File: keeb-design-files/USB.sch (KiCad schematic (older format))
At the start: 35 parts, among them J3 USB_B, J4 S2B-PH-K-S, J5 Conn_01x02, SW71 SW_SPDT, U3 USBLC6-2SC6, U4 BQ24075, U5 NXE2S0505MC, U6 STC3100

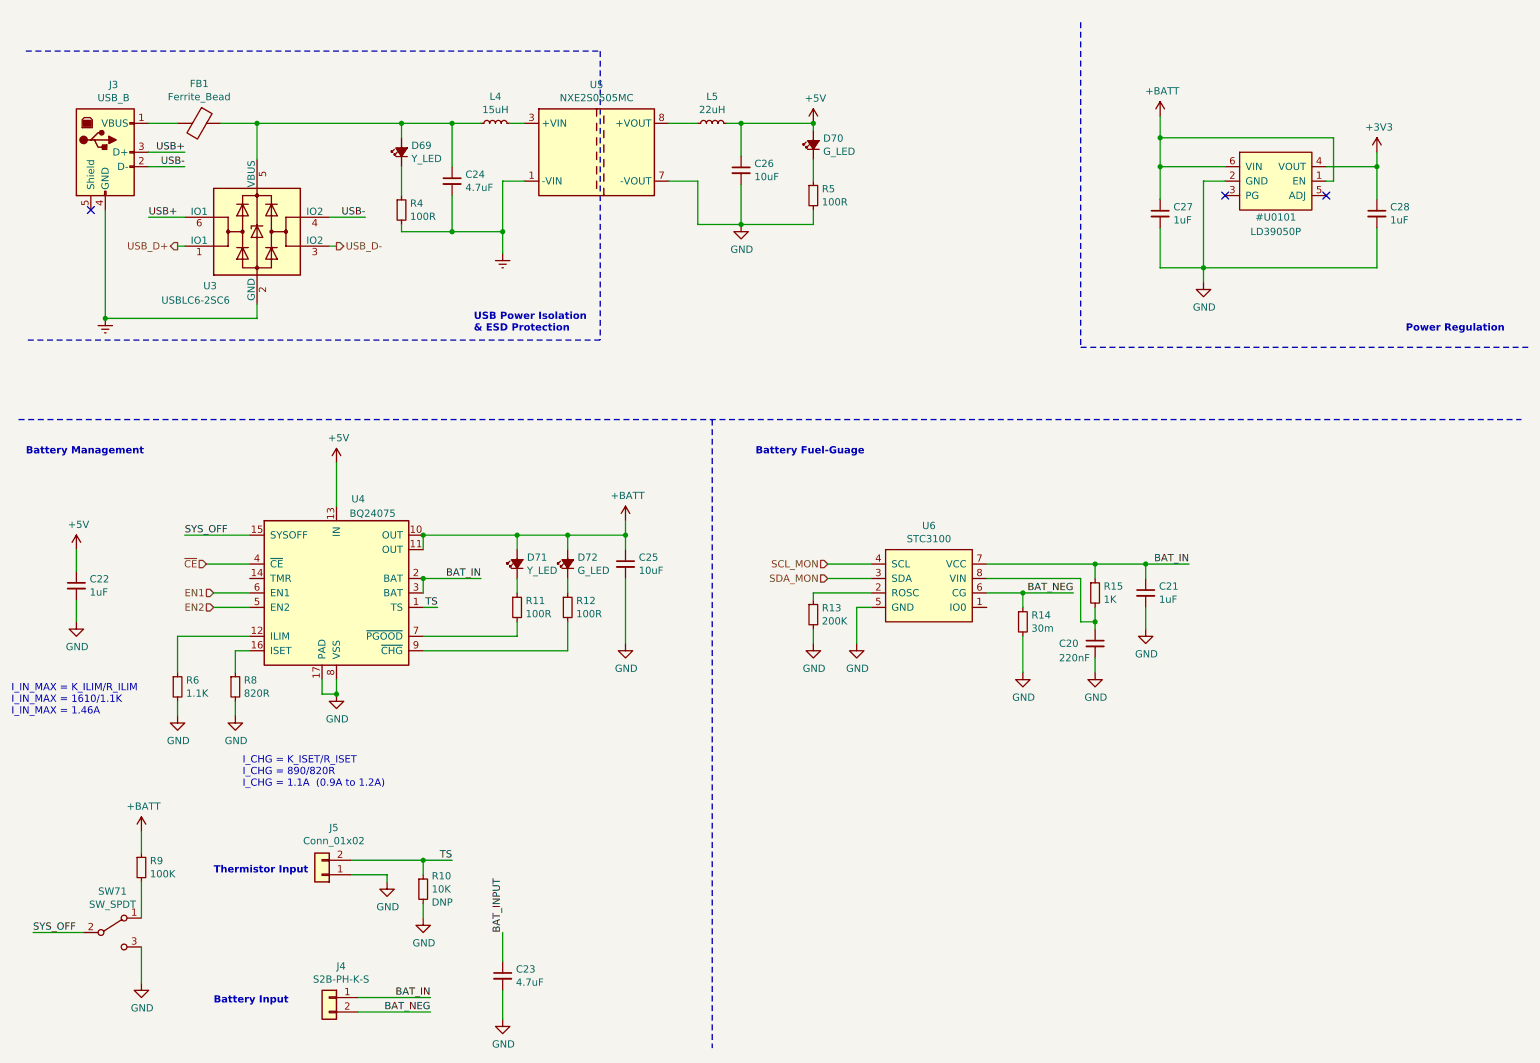
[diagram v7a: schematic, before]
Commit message: Confirm LCSC part numbers, started placement for layout
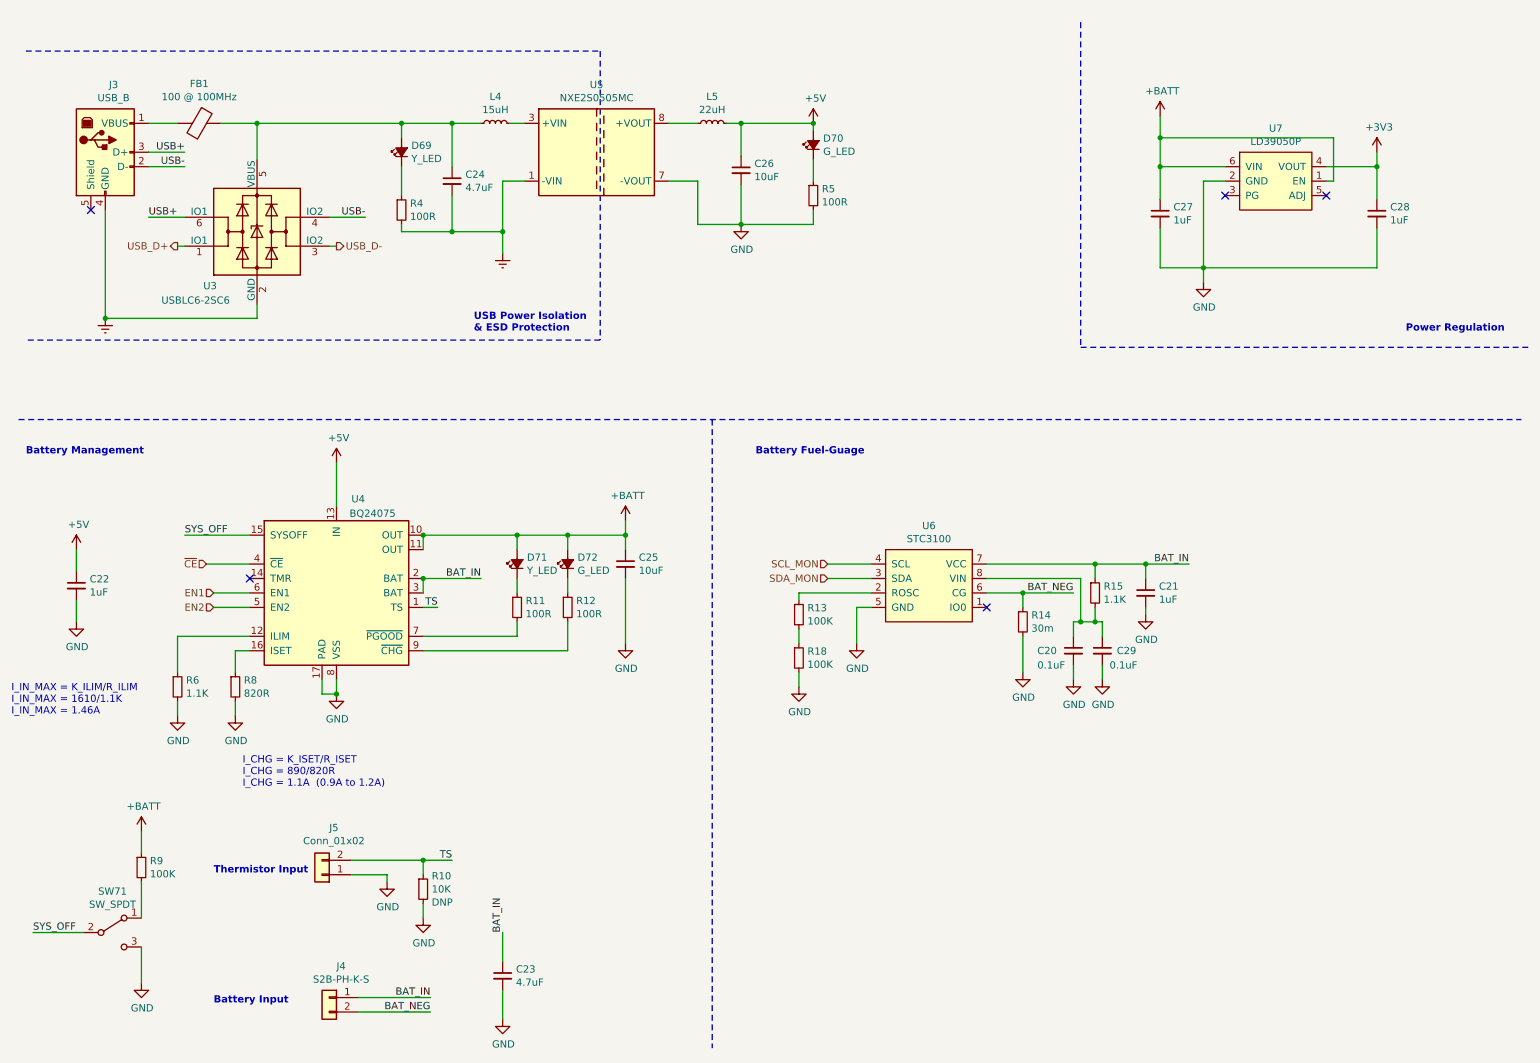
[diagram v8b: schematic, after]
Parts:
- added C29: 0.1uF, Capacitor_SMD:C_0402_1005Metric, symbol Device:C_Small
- added R18: 100K, Resistor_SMD:R_0402_1005Metric, symbol Device:R_Small
- added U7: LD39050P, Package_DFN_QFN:DFN-6-1EP_3x3mm_P0.95mm_EP1.7x2.6mm, symbol LDO:LD39050P
- C20: value 220nF -> 0.1uF; footprint (none) -> Capacitor_SMD:C_0402_1005Metric; LCSC Part Number (none) -> C1525
- C21, C22, C27, C28: footprint (none) -> Capacitor_SMD:C_0402_1005Metric; LCSC Part Number (none) -> C52923
- FB1: value Ferrite_Bead -> 100 @ 100MHz; footprint (none) -> Resistor_SMD:R_0603_1608Metric_Pad1.05x0.95mm_HandSolder
- L4, L5: footprint (none) -> Inductor_SMD:L_Bourns_SRR1260
- R10: footprint (none) -> Resistor_SMD:R_0603_1608Metric_Pad1.05x0.95mm_HandSolder
- R13: value 200K -> 100K; footprint (none) -> Resistor_SMD:R_0402_1005Metric; LCSC Part Number (none) -> C25741
- R15: value 1K -> 1.1K; footprint (none) -> Resistor_SMD:R_0402_1005Metric; LCSC Part Number (none) -> C25860
- R6, R8: footprint (none) -> Resistor_SMD:R_0402_1005Metric
- R9: footprint (none) -> Resistor_SMD:R_0402_1005Metric; LCSC Part Number (none) -> C25741
- U6: footprint (none) -> Package_DFN_QFN:DFN-8-1EP_3x3mm_P0.5mm_EP1.66x2.38mm
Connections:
- net BAT_INPUT is gone; now on net BAT_IN: C23.1
- net +3V3: now also U7.4 (VOUT)
- net +BATT: now also U7.1 (EN), U7.6 (VIN)
- net GND: now also C29.2, R18.2, U7.2 (GND); no longer R13.2
- net at C20.1, R15.2, U6.8 (VIN): now also C29.1
- new net: R13.2, R18.1
- no-connect marks 3 -> 5
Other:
- moved on the sheet: C20, R13
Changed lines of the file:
@@
 	2300 1550 2300 1300
-Wire Wire Line
-	2300 1300 3300 1300
 Wire Wire Line
 	1550 1600 1800 1600
@@
 F 0 "L4" V 4135 1300 50  0000 C CNN
 F 1 "15uH" V 4044 1300 50  0000 C CNN
-F 2 "" H 3950 1300 50  0001 C CNN
+F 2 "Inductor_SMD:L_Bourns_SRR1260" H 3950 1300 50  0001 C CNN
 F 3 "~" H 3950 1300 50  0001 C CNN
 F 4 "C132136" H 3950 1300 50  0001 C CNN "LCSC Part Number"
@@
 F 0 "L5" V 5635 1300 50  0000 C CNN
 F 1 "22uH" V 5544 1300 50  0000 C CNN
-F 2 "" H 5450 1300 50  0001 C CNN
+F 2 "Inductor_SMD:L_Bourns_SRR1260" H 5450 1300 50  0001 C CNN
 F 3 "~" H 5450 1300 50  0001 C CNN
 F 4 "C132137" H 5450 1300 50  0001 C CNN "LCSC Part Number"
@@
 	5650 2000 6150 2000
 $Comp
-L LDO:LD39050P #U0101
-U 1 1 5EBC09BA
-P 9350 1700
-F 0 "#U0101" H 9350 1450 50  0000 C CNN
-F 1 "LD39050P" H 9350 1350 50  0000 C CNN
-F 2 "Package_DFN_QFN:DFN-6-1EP_3x3mm_P0.95mm_EP1.7x2.6mm" H 9350 1250 50  0001 C CNN
-F 3 "https://datasheet.lcsc.com/szlcsc/STMicroelectronics-LD39050PU33R_C132827.pdf" H 9350 1550 50  0001 C CNN
-F 4 "C132827" H 9350 1973 50  0001 C CNN "LCSC Part Number"
-	1    9350 1700
-	1    0    0    -1
-$EndComp
-$Comp
 L power:GND #PWR0132
 U 1 1 5EBC166E
@@
 F 0 "C27" H 8642 1971 50  0000 L CNN
 F 1 "1uF" H 8642 1880 50  0000 L CNN
-F 2 "" H 8550 1925 50  0001 C CNN
+F 2 "Capacitor_SMD:C_0402_1005Metric" H 8550 1925 50  0001 C CNN
 F 3 "~" H 8550 1925 50  0001 C CNN
+F 4 "C52923" H 8550 1925 50  0001 C CNN "LCSC Part Number"
 	1    8550 1925
 	1    0    0    -1
@@
 F 0 "C28" H 10142 1971 50  0000 L CNN
 F 1 "1uF" H 10142 1880 50  0000 L CNN
-F 2 "" H 10050 1925 50  0001 C CNN
+F 2 "Capacitor_SMD:C_0402_1005Metric" H 10050 1925 50  0001 C CNN
 F 3 "~" H 10050 1925 50  0001 C CNN
+F 4 "C52923" H 10050 1925 50  0001 C CNN "LCSC Part Number"
 	1    10050 1925
 	1    0    0    -1
@@
 F 0 "C22" H 1142 4546 50  0000 L CNN
 F 1 "1uF" H 1142 4455 50  0000 L CNN
-F 2 "" H 1050 4500 50  0001 C CNN
+F 2 "Capacitor_SMD:C_0402_1005Metric" H 1050 4500 50  0001 C CNN
 F 3 "~" H 1050 4500 50  0001 C CNN
+F 4 "C52923" H 1050 4500 50  0001 C CNN "LCSC Part Number"
 	1    1050 4500
 	1    0    0    -1
@@
 P 1900 1300
 F 0 "FB1" V 1626 1300 50  0000 C CNN
-F 1 "Ferrite_Bead" V 1717 1300 50  0000 C CNN
-F 2 "" V 1830 1300 50  0001 C CNN
+F 1 "100 @ 100MHz" V 1717 1300 50  0000 C CNN
+F 2 "Resistor_SMD:R_0603_1608Metric_Pad1.05x0.95mm_HandSolder" V 1830 1300 50  0001 C CNN
 F 3 "~" H 1900 1300 50  0001 C CNN
 	1    1900 1300
@@
 F 0 "R9" H 1559 6496 50  0000 L CNN
 F 1 "100K" H 1559 6405 50  0000 L CNN
-F 2 "" H 1500 6450 50  0001 C CNN
+F 2 "Resistor_SMD:R_0402_1005Metric" H 1500 6450 50  0001 C CNN
 F 3 "~" H 1500 6450 50  0001 C CNN
+F 4 "C25741" H 1500 6450 50  0001 C CNN "LCSC Part Number"
 	1    1500 6450
 	1    0    0    -1
@@
 F 0 "R8" H 2209 5246 50  0000 L CNN
 F 1 "820R" H 2209 5155 50  0000 L CNN
-F 2 "" H 2150 5200 50  0001 C CNN
+F 2 "Resistor_SMD:R_0402_1005Metric" H 2150 5200 50  0001 C CNN
 F 3 "~" H 2150 5200 50  0001 C CNN
 F 4 "C25135" H 2209 5109 50  0001 L CNN "LCSC Part Number"
@@
 F 0 "R6" H 1809 5246 50  0000 L CNN
 F 1 "1.1K" H 1809 5155 50  0000 L CNN
-F 2 "" H 1750 5200 50  0001 C CNN
+F 2 "Resistor_SMD:R_0402_1005Metric" H 1750 5200 50  0001 C CNN
 F 3 "~" H 1750 5200 50  0001 C CNN
 F 4 "C25860" H 1750 5200 50  0001 C CNN "LCSC Part Number"
@@
 F 0 "R10" H 3509 6691 50  0000 L CNN
 F 1 "10K" H 3509 6600 50  0000 L CNN
-F 2 "" H 3450 6600 50  0001 C CNN
+F 2 "Resistor_SMD:R_0603_1608Metric_Pad1.05x0.95mm_HandSolder" H 3450 6600 50  0001 C CNN
 F 3 "~" H 3450 6600 50  0001 C CNN
 F 4 "DNP" H 3509 6509 50  0000 L CNN "LCSC Part Number"
@@
 	4000 6900 4000 7100
 Text Label 4000 6900 1    50   ~ 0
-BAT_INPUT
+BAT_IN
 $Comp
 L Device:C_Small C23
@@
 F 0 "U6" H 6950 4915 50  0000 C CNN
 F 1 "STC3100" H 6950 4824 50  0000 C CNN
-F 2 "" H 6950 4500 50  0001 C CNN
+F 2 "Package_DFN_QFN:DFN-8-1EP_3x3mm_P0.5mm_EP1.66x2.38mm" H 6950 4500 50  0001 C CNN
 F 3 "" H 6950 4500 50  0001 C CNN
 	1    6950 4500
@@
 F 0 "C21" H 8542 4596 50  0000 L CNN
 F 1 "1uF" H 8542 4505 50  0000 L CNN
-F 2 "" H 8450 4550 50  0001 C CNN
+F 2 "Capacitor_SMD:C_0402_1005Metric" H 8450 4550 50  0001 C CNN
 F 3 "~" H 8450 4550 50  0001 C CNN
+F 4 "C52923" H 8450 4550 50  0001 C CNN "LCSC Part Number"
 	1    8450 4550
 	1    0    0    -1
@@
 P 8100 4550
 F 0 "R15" H 8159 4596 50  0000 L CNN
-F 1 "1K" H 8159 4505 50  0000 L CNN
-F 2 "" H 8100 4550 50  0001 C CNN
+F 1 "1.1K" H 8159 4505 50  0000 L CNN
+F 2 "Resistor_SMD:R_0402_1005Metric" H 8100 4550 50  0001 C CNN
 F 3 "~" H 8100 4550 50  0001 C CNN
+F 4 "C25860" H 8100 4550 50  0001 C CNN "LCSC Part Number"
 	1    8100 4550
-	1    0    0    -1
-$EndComp
-$Comp
-L Device:C_Small C20
-U 1 1 5ECB4C56
-P 8100 4900
-F 0 "C20" H 7850 4900 50  0000 L CNN
-F 1 "220nF" H 7850 4800 50  0000 L CNN
-F 2 "" H 8100 4900 50  0001 C CNN
-F 3 "~" H 8100 4900 50  0001 C CNN
-	1    8100 4900
 	1    0    0    -1
 $EndComp
@@
 L power:GND #PWR0149
 U 1 1 5ECB563A
-P 8100 5100
-F 0 "#PWR0149" H 8100 4850 50  0001 C CNN
-F 1 "GND" H 8105 4927 50  0000 C CNN
-F 2 "" H 8100 5100 50  0001 C CNN
-F 3 "" H 8100 5100 50  0001 C CNN
-	1    8100 5100
+P 7950 5150
+F 0 "#PWR0149" H 7950 4900 50  0001 C CNN
+F 1 "GND" H 7955 4977 50  0000 C CNN
+F 2 "" H 7950 5150 50  0001 C CNN
+F 3 "" H 7950 5150 50  0001 C CNN
+	1    7950 5150
 	1    0    0    -1
 $EndComp
@@
 Wire Wire Line
 	8100 4650 8100 4750
-Wire Wire Line
-	8100 5000 8100 5100
 $Comp
 L power:GND #PWR0150
 U 1 1 5ECC8420
-P 8450 4800
-F 0 "#PWR0150" H 8450 4550 50  0001 C CNN
-F 1 "GND" H 8455 4627 50  0000 C CNN
-F 2 "" H 8450 4800 50  0001 C CNN
-F 3 "" H 8450 4800 50  0001 C CNN
-	1    8450 4800
-	1    0    0    -1
-$EndComp
-Wire Wire Line
-	8450 4800 8450 4650
+P 8450 4700
+F 0 "#PWR0150" H 8450 4450 50  0001 C CNN
+F 1 "GND" H 8455 4527 50  0000 C CNN
+F 2 "" H 8450 4700 50  0001 C CNN
+F 3 "" H 8450 4700 50  0001 C CNN
+	1    8450 4700
+	1    0    0    -1
+$EndComp
+Wire Wire Line
+	8450 4700 8450 4650
 Wire Wire Line
 	7350 4450 8000 4450
@@
 Wire Wire Line
 	8000 4750 8100 4750
-Connection ~ 8100 4750
-Wire Wire Line
-	8100 4750 8100 4800
 Text HLabel 6250 4350 0    50   Input ~ 0
 SCL_MON
@@
 L Device:R_Small R13
 U 1 1 5ECED1DA
-P 6150 4700
-F 0 "R13" H 6209 4746 50  0000 L CNN
-F 1 "200K" H 6209 4655 50  0000 L CNN
-F 2 "" H 6150 4700 50  0001 C CNN
-F 3 "~" H 6150 4700 50  0001 C CNN
-	1    6150 4700
-	1    0    0    -1
-$EndComp
-Wire Wire Line
-	6150 4600 6150 4550
-Wire Wire Line
-	6150 4550 6550 4550
+P 6050 4700
+F 0 "R13" H 6109 4746 50  0000 L CNN
+F 1 "100K" H 6109 4655 50  0000 L CNN
+F 2 "Resistor_SMD:R_0402_1005Metric" H 6050 4700 50  0001 C CNN
+F 3 "~" H 6050 4700 50  0001 C CNN
+F 4 "C25741" H 6050 4700 50  0001 C CNN "LCSC Part Number"
+	1    6050 4700
+	1    0    0    -1
+$EndComp
+Wire Wire Line
+	6050 4600 6050 4550
+Wire Wire Line
+	6050 4550 6550 4550
 $Comp
 L power:GND #PWR0152
 U 1 1 5ECF1E0E
-P 6150 4900
-F 0 "#PWR0152" H 6150 4650 50  0001 C CNN
-F 1 "GND" H 6155 4727 50  0000 C CNN
-F 2 "" H 6150 4900 50  0001 C CNN
-F 3 "" H 6150 4900 50  0001 C CNN
-	1    6150 4900
-	1    0    0    -1
-$EndComp
-Wire Wire Line
-	6150 4800 6150 4900
+P 6050 5200
+F 0 "#PWR0152" H 6050 4950 50  0001 C CNN
+F 1 "GND" H 6055 5027 50  0000 C CNN
+F 2 "" H 6050 5200 50  0001 C CNN
+F 3 "" H 6050 5200 50  0001 C CNN
+	1    6050 5200
+	1    0    0    -1
+$EndComp
 Text Notes 5750 3600 0    50   ~ 10
 Battery Fuel-Guage
@@
 	3450 4450 3850 4450
 Connection ~ 3450 4450
+$Comp
+L Device:C_Small C29
+U 1 1 5EC7E653
+P 8150 4950
+F 0 "C29" H 8250 4950 50  0000 L CNN
+F 1 "0.1uF" H 8200 4850 50  0000 L CNN
+F 2 "Capacitor_SMD:C_0402_1005Metric" H 8150 4950 50  0001 C CNN
+F 3 "~" H 8150 4950 50  0001 C CNN
+F 4 "C1525" H 8150 4950 50  0001 C CNN "LCSC Part Number"
+	1    8150 4950
+	1    0    0    -1
+$EndComp
+$Comp
+L power:GND #PWR0157
+U 1 1 5EC9C4D0
+P 8150 5150
+F 0 "#PWR0157" H 8150 4900 50  0001 C CNN
+F 1 "GND" H 8155 4977 50  0000 C CNN
+F 2 "" H 8150 5150 50  0001 C CNN
+F 3 "" H 8150 5150 50  0001 C CNN
+	1    8150 5150
+	1    0    0    -1
+$EndComp
+Wire Wire Line
+	8150 5150 8150 5050
+Connection ~ 8000 4750
+Wire Wire Line
+	7950 4750 8000 4750
+Wire Wire Line
+	7950 5050 7950 5150
+Wire Wire Line
+	7950 4850 7950 4750
+$Comp
+L Device:C_Small C20
+U 1 1 5ECB4C56
+P 7950 4950
+F 0 "C20" H 7700 4950 50  0000 L CNN
+F 1 "0.1uF" H 7700 4850 50  0000 L CNN
+F 2 "Capacitor_SMD:C_0402_1005Metric" H 7950 4950 50  0001 C CNN
+F 3 "~" H 7950 4950 50  0001 C CNN
+F 4 "C1525" H 7950 4950 50  0001 C CNN "LCSC Part Number"
+	1    7950 4950
+	1    0    0    -1
+$EndComp
+Wire Wire Line
+	8100 4750 8150 4750
+Wire Wire Line
+	8150 4750 8150 4850
+Connection ~ 8100 4750
+$Comp
+L Device:R_Small R18
+U 1 1 5ED54916
+P 6050 5000
+F 0 "R18" H 6109 5046 50  0000 L CNN
+F 1 "100K" H 6109 4955 50  0000 L CNN
+F 2 "Resistor_SMD:R_0402_1005Metric" H 6050 5000 50  0001 C CNN
+F 3 "~" H 6050 5000 50  0001 C CNN
+F 4 "C25741" H 6050 5000 50  0001 C CNN "LCSC Part Number"
+	1    6050 5000
+	1    0    0    -1
+$EndComp
+Wire Wire Line
+	6050 4800 6050 4900
+Wire Wire Line
+	6050 5100 6050 5200
+NoConn ~ 2250 4450
+NoConn ~ 7350 4650
+Wire Wire Line
+	2300 1300 3300 1300
+$Comp
+L LDO:LD39050P U7
+U 1 1 5ED4AB70
+P 9350 1700
+F 0 "U7" H 9350 2065 50  0000 C CNN
+F 1 "LD39050P" H 9350 1974 50  0000 C CNN
+F 2 "Package_DFN_QFN:DFN-6-1EP_3x3mm_P0.95mm_EP1.7x2.6mm" H 9350 1250 50  0001 C CNN
+F 3 "https://datasheet.lcsc.com/szlcsc/STMicroelectronics-LD39050PU33R_C132827.pdf" H 9350 1550 50  0001 C CNN
+	1    9350 1700
+	1    0    0    -1
+$EndComp
 $EndSCHEMATC
